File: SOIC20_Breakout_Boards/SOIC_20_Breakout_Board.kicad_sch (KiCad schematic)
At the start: 6 parts, among them J1 Conn_01x10, J2 Conn_01x10, J3 Conn_01x01, J4 Conn_01x01

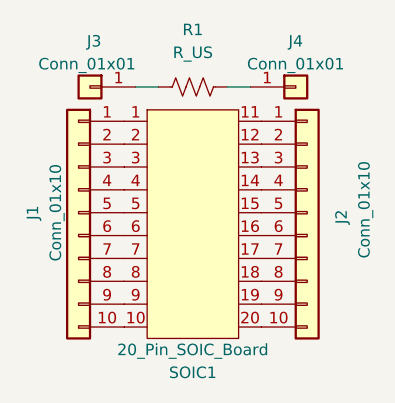
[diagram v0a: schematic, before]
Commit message: Created PCB designs for the 14, 16 & 20 pic SOIC's
Finalized and committed pcb designs for the 14, 16, and 20 SOIC breakout boards
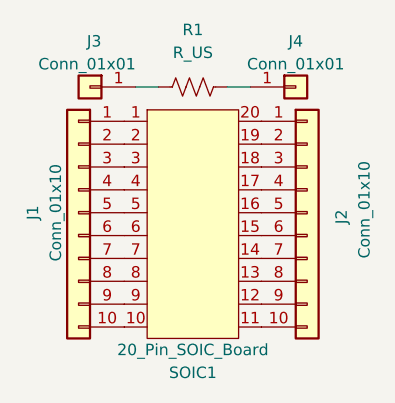
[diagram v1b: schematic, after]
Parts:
- J1, J2: footprint (none) -> Connector_PinSocket_2.54mm:PinSocket_1x10_P2.54mm_Vertical
- SOIC1: footprint (none) -> SOIC_Footprints:20_Pin_SOIC_Board
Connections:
- net at SOIC1.11: now also J2.10 (Pin_10); no longer J2.1 (Pin_1)
- net at SOIC1.20: now also J2.1 (Pin_1); no longer J2.10 (Pin_10)
- net at SOIC1.12: now also J2.9 (Pin_9); no longer J2.2 (Pin_2)
- net at SOIC1.13: now also J2.8 (Pin_8); no longer J2.3 (Pin_3)
- net at SOIC1.14: now also J2.7 (Pin_7); no longer J2.4 (Pin_4)
- net at SOIC1.15: now also J2.6 (Pin_6); no longer J2.5 (Pin_5)
- net at SOIC1.16: now also J2.5 (Pin_5); no longer J2.6 (Pin_6)
- net at SOIC1.17: now also J2.4 (Pin_4); no longer J2.7 (Pin_7)
- net at SOIC1.18: now also J2.3 (Pin_3); no longer J2.8 (Pin_8)
- net at SOIC1.19: now also J2.2 (Pin_2); no longer J2.9 (Pin_9)
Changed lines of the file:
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@@
     (pin "1")
+  )
+  (symbol (lib_id "8_Pin_SOIC_Board:20_Pin_SOIC_Board") (at 125.73 104.14 0) (unit 1)
+    (in_bom yes) (on_board yes)
+    (property "Reference" "SOIC1" (id 0) (at 125.73 123.19 0))
+    (property "Value" "20_Pin_SOIC_Board" (id 1) (at 125.73 120.65 0))
+    (property "Footprint" "SOIC_Footprints:20_Pin_SOIC_Board" (id 2) (at 125.73 104.14 0)
+      (effects (font (size 1.27 1.27)) hide)
+    )
+    (property "Datasheet" "" (id 3) (at 125.73 104.14 0)
+      (effects (font (size 1.27 1.27)) hide)
+    )
+    (pin "1")
+    (pin "10")
+    (pin "11")
+    (pin "12")
+    (pin "13")
+    (pin "14")
+    (pin "15")
+    (pin "16")
+    (pin "17")
+    (pin "18")
+    (pin "19")
+    (pin "2")
+    (pin "20")
+    (pin "3")
+    (pin "4")
+    (pin "5")
+    (pin "6")
+    (pin "7")
+    (pin "8")
+    (pin "9")
   )
   (symbol (lib_id "Connector_Generic:Conn_01x10") (at 138.43 105.41 0) (unit 1)
@@
       (effects (font (size 1.27 1.27)) (justify left))
     )
-    (property "Footprint" "" (id 2) (at 138.43 105.41 0)
+    (property "Footprint" "Connector_PinSocket_2.54mm:PinSocket_1x10_P2.54mm_Vertical" (id 2) (at 138.43 105.41 0)
       (effects (font (size 1.27 1.27)) hide)
     )
@@
     (property "Reference" "J1" (id 0) (at 107.95 105.41 90))
     (property "Value" "Conn_01x10" (id 1) (at 110.49 105.41 90))
-    (property "Footprint" "" (id 2) (at 113.03 105.41 0)
+    (property "Footprint" "Connector_PinSocket_2.54mm:PinSocket_1x10_P2.54mm_Vertical" (id 2) (at 113.03 105.41 0)
       (effects (font (size 1.27 1.27)) hide)
     )
@@
     (pin "1")
   )
-  (symbol (lib_id "8_Pin_SOIC_Board:20_Pin_SOIC_Board") (at 125.73 104.14 0) (unit 1)
-    (in_bom yes) (on_board yes)
-    (property "Reference" "SOIC1" (id 0) (at 125.73 123.19 0))
-    (property "Value" "20_Pin_SOIC_Board" (id 1) (at 125.73 120.65 0))
-    (property "Footprint" "" (id 2) (at 125.73 104.14 0)
-      (effects (font (size 1.27 1.27)) hide)
-    )
-    (property "Datasheet" "" (id 3) (at 125.73 104.14 0)
-      (effects (font (size 1.27 1.27)) hide)
-    )
-    (pin "1")
-    (pin "10")
-    (pin "11")
-    (pin "12")
-    (pin "13")
-    (pin "14")
-    (pin "15")
-    (pin "16")
-    (pin "17")
-    (pin "18")
-    (pin "19")
-    (pin "2")
-    (pin "20")
-    (pin "3")
-    (pin "4")
-    (pin "5")
-    (pin "6")
-    (pin "7")
-    (pin "8")
-    (pin "9")
-  )
   (symbol (lib_id "Device:R_US") (at 125.73 91.44 270) (unit 1)
     (in_bom yes) (on_board yes) (fields_autoplaced)
@@
   (symbol_instances
     (path "/7cefbcab-8288-45c8-89ea-9d379e052e64"
-      (reference "J1") (unit 1) (value "Conn_01x10") (footprint "")
+      (reference "J1") (unit 1) (value "Conn_01x10") (footprint "Connector_PinSocket_2.54mm:PinSocket_1x10_P2.54mm_Vertical")
     )
     (path "/5e1238bb-529b-4245-a5ea-b640a2cedb8b"
-      (reference "J2") (unit 1) (value "Conn_01x10") (footprint "")
+      (reference "J2") (unit 1) (value "Conn_01x10") (footprint "Connector_PinSocket_2.54mm:PinSocket_1x10_P2.54mm_Vertical")
     )
     (path "/7dfc8e4d-cb13-4be6-bcf8-32029bab029b"
@@
       (reference "R1") (unit 1) (value "R_US") (footprint "Resistor_SMD:R_0805_2012Metric")
     )
-    (path "/8a9ad629-474b-4b7b-a3af-4e2496391838"
-      (reference "SOIC1") (unit 1) (value "20_Pin_SOIC_Board") (footprint "")
+    (path "/46adb454-755c-4cb3-b417-44ee32517280"
+      (reference "SOIC1") (unit 1) (value "20_Pin_SOIC_Board") (footprint "SOIC_Footprints:20_Pin_SOIC_Board")
     )
   )
